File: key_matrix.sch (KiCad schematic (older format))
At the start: 168 parts

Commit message: Add LED controller + LEDS
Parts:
- added unit 2 of K_0_0
- added unit 2 of K_1_0
- added unit 2 of K_2_0
- added unit 2 of K_3_0
- added unit 2 of K_4_0
- added unit 2 of K_5_0
- added unit 2 of K_6_0
- added unit 2 of K_7_0
- added unit 2 of K_8_0
- added unit 2 of K_9_0
- added unit 2 of K_ALT1_0
- added unit 2 of K_ALT_0
- added unit 2 of K_A_0
- added unit 2 of K_BACKSPACE_0
- added unit 2 of K_BSLSH_0
- added unit 2 of K_B_0
- added unit 2 of K_CAPS_LOCK_0
- added unit 2 of K_COMMA_0
- added unit 2 of K_CTRL1_0
- added unit 2 of K_CTRL_0
- added unit 2 of K_C_0
- added unit 2 of K_DOT_0
- added unit 2 of K_DOWN_0
- added unit 2 of K_D_0
- added unit 2 of K_END_0
- added unit 2 of K_ENTER_0
- added unit 2 of K_EQUAL_0
- added unit 2 of K_ESC_0
- added unit 2 of K_E_0
- added unit 2 of K_F10_0
- added unit 2 of K_F11_0
- added unit 2 of K_F12_0
- added unit 2 of K_F1_0
- added unit 2 of K_F2_0
- added unit 2 of K_F3_0
- added unit 2 of K_F4_0
- added unit 2 of K_F5_0
- added unit 2 of K_F6_0
- added unit 2 of K_F7_0
- added unit 2 of K_F8_0
- added unit 2 of K_F9_0
- added unit 2 of K_FN_0
- added unit 2 of K_F_0
- added unit 2 of K_G_0
- added unit 2 of K_HOME_0
- added unit 2 of K_H_0
- added unit 2 of K_INSERT_0
- added unit 2 of K_I_0
- added unit 2 of K_J_0
- added unit 2 of K_K_0
- added unit 2 of K_LEFT_0
- added unit 2 of K_L_0
- added unit 2 of K_MINUS_0
- added unit 2 of K_M_0
- added unit 2 of K_NMLK_0
- added unit 2 of K_N_0
- added unit 2 of K_O_0
- added unit 2 of K_PAGE_DOWN_0
- added unit 2 of K_PAGE_UP_0
- added unit 2 of K_P_0
- added unit 2 of K_QUOTE_0
- added unit 2 of K_Q_0
- added unit 2 of K_RIGHT_0
- added unit 2 of K_R_0
- added unit 2 of K_SCRLK_0
- added unit 2 of K_SEMIC_0
- added unit 2 of K_SHIFT1_0
- added unit 2 of K_SHIFT_0
- added unit 2 of K_SLASH_0
- added unit 2 of K_SPC_0
- added unit 2 of K_S_0
- added unit 2 of K_TAB_0
- added unit 2 of K_T_0
- added unit 2 of K_UP_0
- added unit 2 of K_U_0
- added unit 2 of K_V_0
- added unit 2 of K_WIN_0
- added unit 2 of K_W_0
- added unit 2 of K_X_0
- added unit 2 of K_Y_0
- added unit 2 of K_Z_0
- added unit 2 of K_[_0
- added unit 2 of K_]_0
- added unit 2 of K_`_0
- K_0_0, K_1_0, K_2_0, K_3_0, K_4_0, K_5_0, K_6_0, K_7_0, K_8_0, K_9_0, K_ALT1_0, K_A_0, K_B_0, K_COMMA_0, K_CTRL1_0, K_C_0, K_DOT_0, K_DOWN_0, K_D_0, K_END_0, K_EQUAL_0, K_ESC_0, K_E_0, K_F10_0, K_F11_0, K_F12_0, K_F1_0, K_F2_0, K_F3_0, K_F4_0, K_F5_0, K_F6_0, K_F7_0, K_F8_0, K_F9_0, K_FN_0, K_F_0, K_G_0, K_HOME_0, K_H_0, K_INSERT_0, K_I_0, K_J_0, K_K_0, K_LEFT_0, K_L_0, K_MINUS_0, K_M_0, K_NMLK_0, K_N_0, K_O_0, K_PAGE_DOWN_0, K_PAGE_UP_0, K_P_0, K_QUOTE_0, K_Q_0, K_RIGHT_0, K_R_0, K_SCRLK_0, K_SEMIC_0, K_SLASH_0, K_S_0, K_T_0, K_UP_0, K_U_0, K_V_0, K_W_0, K_X_0, K_Y_0, K_Z_0, K_[_0, K_]_0, K_`_0: footprint MX_Alps_Hybrid:MX-1U-NoLED -> MX_Alps_Hybrid:MX-1U
- K_ALT_0, K_CTRL_0, K_WIN_0: footprint MX_Alps_Hybrid:MX-1.25U-NoLED -> MX_Alps_Hybrid:MX-1.25U
- K_BACKSPACE_0: footprint MX_Alps_Hybrid:MX-2U-NoLED -> MX_Alps_Hybrid:MX-2U
- K_BSLSH_0, K_TAB_0: footprint MX_Alps_Hybrid:MX-1.5U-NoLED -> MX_Alps_Hybrid:MX-1.5U
- K_CAPS_LOCK_0, K_SHIFT1_0: footprint MX_Alps_Hybrid:MX-1.75U-NoLED -> MX_Alps_Hybrid:MX-1.75U
- K_ENTER_0, K_SHIFT_0: footprint MX_Alps_Hybrid:MX-2.25U-NoLED -> MX_Alps_Hybrid:MX-2.25U
- K_SPC_0: footprint MX_Alps_Hybrid:MX-6.25U-NoLED -> MX_Alps_Hybrid:MX-6.25U
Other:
- note added: "White LEDs, approx 3.3V Vf"

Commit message: Wire LEDs into controller
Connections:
- net LED_CB2: now reaches K_L_0.3 (A)
- net LED_CB2: now also K_0_0.4 (K), K_8_0.4 (K), K_9_0.4 (K), K_BACKSPACE_0.4 (K), K_DOT_0.3 (A), K_EQUAL_0.4 (K), K_F8_0.3 (A), K_HOME_0.4 (K), K_MINUS_0.4 (K), K_O_0.3 (A), K_RIGHT_0.3 (A)
- net LED_CB4: now reaches K_L_0.4 (K)
- net LED_CB4: now also K_0_0.3 (A), K_ENTER_0.4 (K), K_F10_0.3 (A), K_K_0.4 (K), K_PAGE_DOWN_0.4 (K), K_P_0.3 (A), K_QUOTE_0.4 (K), K_SEMIC_0.4 (K), K_SHIFT1_0.3 (A)
- net LED_CA9: now reaches K_M_0.3 (A)
- net LED_CA9: now also K_7_0.3 (A), K_F7_0.3 (A), K_J_0.3 (A), K_LEFT_0.3 (A), K_U_0.3 (A)
- net LED_CA5: now reaches K_M_0.4 (K)
- net LED_CA5: now also K_3_0.3 (A), K_ALT1_0.3 (A), K_B_0.4 (K), K_C_0.4 (K), K_D_0.3 (A), K_E_0.3 (A), K_F3_0.3 (A), K_N_0.4 (K), K_SHIFT_0.4 (K), K_V_0.4 (K), K_X_0.4 (K), K_Z_0.4 (K)
- net LED_CB3: now reaches K_O_0.4 (K)
- net LED_CB3: now also K_9_0.3 (A), K_BSLSH_0.4 (K), K_F9_0.3 (A), K_I_0.4 (K), K_PAGE_UP_0.4 (K), K_P_0.4 (K), K_SEMIC_0.3 (A), K_SLASH_0.3 (A), K_[_0.4 (K), K_]_0.4 (K)
- net LED_CB1: now reaches K_COMMA_0.3 (A)
- net LED_CB1: now also K_8_0.3 (A), K_DOWN_0.3 (A), K_F10_0.4 (K), K_F11_0.4 (K), K_F12_0.4 (K), K_F8_0.4 (K), K_F9_0.4 (K), K_INSERT_0.4 (K), K_I_0.3 (A), K_K_0.3 (A), K_NMLK_0.4 (K), K_SCRLK_0.4 (K)
- net LED_CB5: now reaches K_COMMA_0.4 (K)
- net LED_CB5: now also K_DOT_0.4 (K), K_END_0.4 (K), K_F11_0.3 (A), K_MINUS_0.3 (A), K_QUOTE_0.3 (A), K_SHIFT1_0.4 (K), K_SLASH_0.4 (K), K_UP_0.4 (K), K_[_0.3 (A)
- net LED_CA8: now reaches K_N_0.3 (A)
- net LED_CA8: now also K_6_0.3 (A), K_CTRL1_0.3 (A), K_F6_0.3 (A), K_H_0.3 (A), K_Y_0.3 (A)
- net LED_CA2: now reaches K_Z_0.3 (A)
- net LED_CA2: now also K_1_0.4 (K), K_2_0.4 (K), K_3_0.4 (K), K_4_0.4 (K), K_5_0.4 (K), K_6_0.4 (K), K_7_0.4 (K), K_A_0.3 (A), K_ESC_0.3 (A), K_Q_0.3 (A), K_WIN_0.3 (A), K_`_0.4 (K)
- net LED_CA3: now reaches K_F1_0.3 (A)
- net LED_CA3: now also K_1_0.3 (A), K_ALT_0.3 (A), K_E_0.4 (K), K_Q_0.4 (K), K_R_0.4 (K), K_S_0.3 (A), K_TAB_0.4 (K), K_T_0.4 (K), K_U_0.4 (K), K_W_0.4 (K), K_X_0.3 (A), K_Y_0.4 (K)
- net LED_CA1: now reaches K_F1_0.4 (K)
- net LED_CA1: now also K_CAPS_LOCK_0.3 (A), K_CTRL_0.3 (A), K_ESC_0.4 (K), K_F2_0.4 (K), K_F3_0.4 (K), K_F4_0.4 (K), K_F5_0.4 (K), K_F6_0.4 (K), K_F7_0.4 (K), K_SHIFT_0.3 (A), K_TAB_0.3 (A), K_`_0.3 (A)
- net LED_CA7: now reaches K_B_0.3 (A)
- net LED_CA7: now also K_5_0.3 (A), K_F5_0.3 (A), K_FN_0.3 (A), K_G_0.3 (A), K_T_0.3 (A)
- net LED_CA6: now reaches K_V_0.3 (A)
- net LED_CA6: now also K_4_0.3 (A), K_ALT1_0.4 (K), K_ALT_0.4 (K), K_CTRL1_0.4 (K), K_CTRL_0.4 (K), K_F4_0.3 (A), K_FN_0.4 (K), K_F_0.3 (A), K_LEFT_0.4 (K), K_R_0.3 (A), K_SPC_0.4 (K), K_WIN_0.4 (K)
- net LED_CA4: now reaches K_C_0.3 (A)
- net LED_CA4: now also K_2_0.3 (A), K_A_0.4 (K), K_CAPS_LOCK_0.4 (K), K_D_0.4 (K), K_F2_0.3 (A), K_F_0.4 (K), K_G_0.4 (K), K_H_0.4 (K), K_J_0.4 (K), K_SPC_0.3 (A), K_S_0.4 (K), K_W_0.3 (A)
- net LED_CB6: now reaches K_UP_0.3 (A)
- net LED_CB6: now also K_DOWN_0.4 (K), K_ENTER_0.3 (A), K_EQUAL_0.3 (A), K_F12_0.3 (A), K_RIGHT_0.4 (K), K_]_0.3 (A)
- net LED_CB7: now reaches K_END_0.3 (A)
- net LED_CB7: now also K_BACKSPACE_0.3 (A), K_BSLSH_0.3 (A), K_PAGE_DOWN_0.3 (A), K_SCRLK_0.3 (A)
- net LED_CB8: now reaches K_PAGE_UP_0.3 (A)
- net LED_CB8: now also K_HOME_0.3 (A), K_NMLK_0.3 (A)
- net LED_CB9: now reaches K_INSERT_0.3 (A)

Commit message: Ripup all traces, rewire schematic matrix to better fit pcb layout
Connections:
- net LED_CA2: no longer K_A_0.3 (A), K_Q_0.3 (A), K_Z_0.3 (A)
- net LED_CA3: now also K_A_0.3 (A), K_Z_0.3 (A); no longer K_S_0.3 (A), K_U_0.4 (K), K_X_0.3 (A)
- net LED_CA4: now also K_Q_0.3 (A), K_X_0.3 (A); no longer K_C_0.3 (A), K_J_0.4 (K), K_SPC_0.3 (A), K_W_0.3 (A)
- net LED_CA5: now also K_S_0.3 (A), K_W_0.3 (A); no longer K_ALT1_0.3 (A), K_D_0.3 (A), K_E_0.3 (A), K_M_0.4 (K)
- net LED_CA6: now also K_C_0.3 (A), K_D_0.3 (A), K_E_0.3 (A); no longer K_ALT1_0.4 (K), K_CTRL1_0.4 (K), K_FN_0.4 (K), K_F_0.3 (A), K_LEFT_0.4 (K), K_R_0.3 (A), K_V_0.3 (A)
- net LED_CA7: now also K_F_0.3 (A), K_R_0.3 (A), K_V_0.3 (A); no longer K_B_0.3 (A), K_FN_0.3 (A), K_G_0.3 (A), K_T_0.3 (A)
- net LED_CA8: now also K_B_0.3 (A), K_G_0.3 (A), K_SPC_0.3 (A), K_T_0.3 (A); no longer K_CTRL1_0.3 (A), K_H_0.3 (A), K_N_0.3 (A), K_Y_0.3 (A)
- net LED_CA9: now also K_H_0.3 (A), K_N_0.3 (A), K_Y_0.3 (A); no longer K_J_0.3 (A), K_LEFT_0.3 (A), K_M_0.3 (A), K_U_0.3 (A)
- net LED_CB1: now also K_J_0.3 (A), K_M_0.3 (A), K_U_0.3 (A); no longer K_COMMA_0.3 (A), K_DOWN_0.3 (A), K_I_0.3 (A), K_K_0.3 (A)
- net LED_CB2: now also K_COMMA_0.3 (A), K_I_0.3 (A), K_K_0.3 (A); no longer K_DOT_0.3 (A), K_L_0.3 (A), K_O_0.3 (A), K_RIGHT_0.3 (A)
- net LED_CB3: now also K_ALT1_0.3 (A), K_DOT_0.3 (A), K_L_0.3 (A), K_U_0.4 (K); no longer K_SEMIC_0.3 (A), K_SLASH_0.3 (A)
- net LED_CB4: now also K_FN_0.3 (A), K_J_0.4 (K), K_O_0.3 (A), K_SLASH_0.3 (A); no longer K_P_0.3 (A), K_SHIFT1_0.3 (A)
- net LED_CB5: now also K_CTRL1_0.3 (A), K_M_0.4 (K), K_P_0.3 (A), K_SEMIC_0.3 (A); no longer K_QUOTE_0.3 (A), K_[_0.3 (A)
- net LED_CB6: now also K_ALT1_0.4 (K), K_CTRL1_0.4 (K), K_FN_0.4 (K), K_LEFT_0.4 (K), K_QUOTE_0.3 (A), K_[_0.3 (A); no longer K_ENTER_0.3 (A), K_UP_0.3 (A), K_]_0.3 (A)
- net LED_CB7: now also K_LEFT_0.3 (A), K_SHIFT1_0.3 (A), K_]_0.3 (A); no longer K_BACKSPACE_0.3 (A), K_BSLSH_0.3 (A), K_END_0.3 (A), K_PAGE_DOWN_0.3 (A)
- net LED_CB8: now also K_BACKSPACE_0.3 (A), K_BSLSH_0.3 (A), K_DOWN_0.3 (A), K_ENTER_0.3 (A), K_UP_0.3 (A); no longer K_HOME_0.3 (A), K_PAGE_UP_0.3 (A)
- net LED_CB9: now also K_END_0.3 (A), K_HOME_0.3 (A), K_PAGE_DOWN_0.3 (A), K_PAGE_UP_0.3 (A), K_RIGHT_0.3 (A)
- net col1: no longer K_A_0.1, K_Q_0.1, K_Z_0.1
- net col10: now also K_ALT1_0.1, K_DOT_0.1, K_L_0.1, K_O_0.1; no longer K_P_0.1, K_SEMIC_0.1, K_SLASH_0.1
- net col11: now also K_FN_0.1, K_P_0.1, K_SEMIC_0.1, K_SLASH_0.1; no longer K_QUOTE_0.1, K_SHIFT1_0.1, K_[_0.1
- net col12: now also K_CTRL1_0.1, K_QUOTE_0.1, K_[_0.1; no longer K_ENTER_0.1, K_UP_0.1, K_]_0.1
- net col13: now also K_LEFT_0.1, K_SHIFT1_0.1, K_]_0.1; no longer K_BACKSPACE_0.1, K_BSLSH_0.1, K_END_0.1, K_PAGE_DOWN_0.1
- net col14: now also K_BACKSPACE_0.1, K_BSLSH_0.1, K_DOWN_0.1, K_ENTER_0.1, K_UP_0.1; no longer K_HOME_0.1, K_PAGE_UP_0.1
- net col15: now also K_END_0.1, K_HOME_0.1, K_PAGE_DOWN_0.1, K_PAGE_UP_0.1, K_RIGHT_0.1
- net col2: now also K_A_0.1, K_Q_0.1, K_Z_0.1; no longer K_S_0.1, K_W_0.1, K_X_0.1
- net col3: now also K_S_0.1, K_W_0.1, K_X_0.1; no longer K_C_0.1, K_D_0.1, K_E_0.1, K_SPC_0.1
- net col4: now also K_C_0.1, K_D_0.1, K_E_0.1; no longer K_ALT1_0.1, K_F_0.1, K_R_0.1, K_V_0.1
- net col5: now also K_F_0.1, K_R_0.1, K_V_0.1; no longer K_B_0.1, K_FN_0.1, K_G_0.1, K_T_0.1
- net col6: now also K_B_0.1, K_G_0.1, K_SPC_0.1, K_T_0.1; no longer K_CTRL1_0.1, K_H_0.1, K_N_0.1, K_Y_0.1
- net col7: now also K_H_0.1, K_N_0.1, K_Y_0.1; no longer K_J_0.1, K_LEFT_0.1, K_M_0.1, K_U_0.1
- net col8: now also K_J_0.1, K_M_0.1, K_U_0.1; no longer K_COMMA_0.1, K_DOWN_0.1, K_I_0.1, K_K_0.1
- net col9: now also K_COMMA_0.1, K_I_0.1, K_K_0.1; no longer K_DOT_0.1, K_L_0.1, K_O_0.1, K_RIGHT_0.1
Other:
- moved on the sheet: D_ALT1_0, D_A_0, D_BACKSPACE_0, D_BSLSH_0, D_B_0, D_COMMA_0, D_CTRL1_0, D_C_0, D_DOT_0, D_DOWN_0, D_D_0, D_END_0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

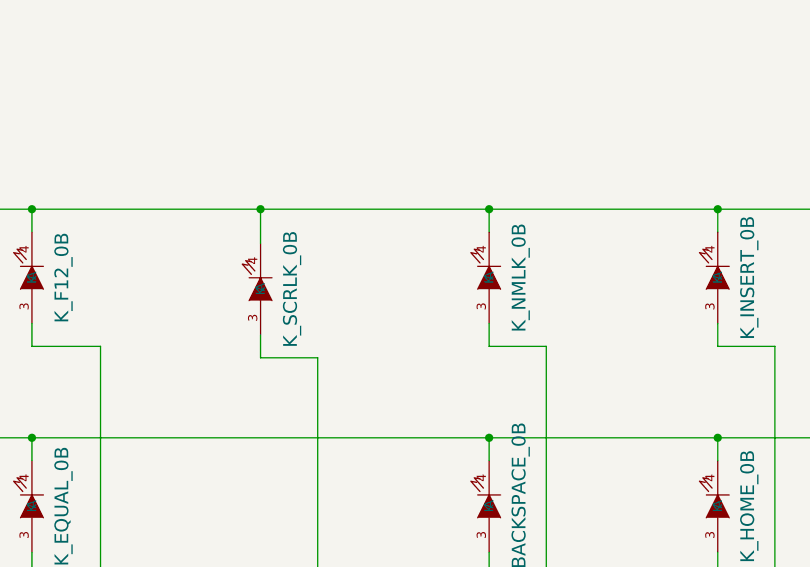
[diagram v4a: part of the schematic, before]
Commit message: Rewire as 4 layer board
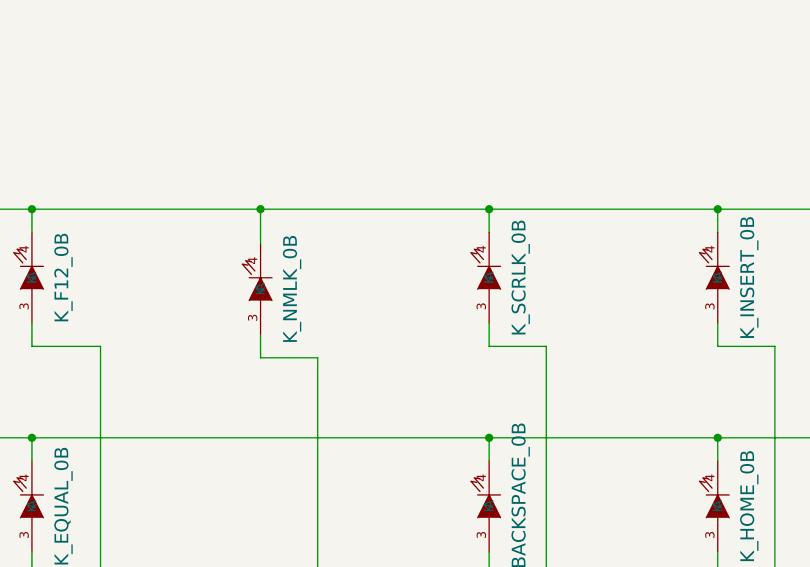
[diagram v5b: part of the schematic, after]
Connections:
- net LED_CB7: now also K_NMLK_0.3 (A); no longer K_SCRLK_0.3 (A)
- net LED_CB8: now also K_SCRLK_0.3 (A); no longer K_NMLK_0.3 (A)
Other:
- moved on the sheet: K_NMLK_0B, K_SCRLK_0B
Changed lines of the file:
@@
 L keyboard_parts:KEYSW K_SCRLK_0
 U 2 1 5E754C95
+P 16000 9250
+F 0 "K_SCRLK_0" H 16000 9381 60  0000 C CNN
+F 1 "KEYSW" H 16000 9100 60  0001 C CNN
+F 2 "MX_Alps_Hybrid:MX-1U" H 16000 9250 60  0001 C CNN
+F 3 "" H 16000 9250 60  0000 C CNN
+	2    16000 9250
+	0    1    1    0
+$EndComp
+$Comp
+L keyboard_parts:KEYSW K_NMLK_0
+U 2 1 5E754C97
 P 15000 9300
-F 0 "K_SCRLK_0" H 15000 9431 60  0000 C CNN
+F 0 "K_NMLK_0" H 15000 9431 60  0000 C CNN
 F 1 "KEYSW" H 15000 9150 60  0001 C CNN
 F 2 "MX_Alps_Hybrid:MX-1U" H 15000 9300 60  0001 C CNN
@@
 	0    1    1    0
 $EndComp
-$Comp
-L keyboard_parts:KEYSW K_NMLK_0
-U 2 1 5E754C97
-P 16000 9250
-F 0 "K_NMLK_0" H 16000 9381 60  0000 C CNN
-F 1 "KEYSW" H 16000 9100 60  0001 C CNN
-F 2 "MX_Alps_Hybrid:MX-1U" H 16000 9250 60  0001 C CNN
-F 3 "" H 16000 9250 60  0000 C CNN
-	2    16000 9250
-	0    1    1    0
-$EndComp

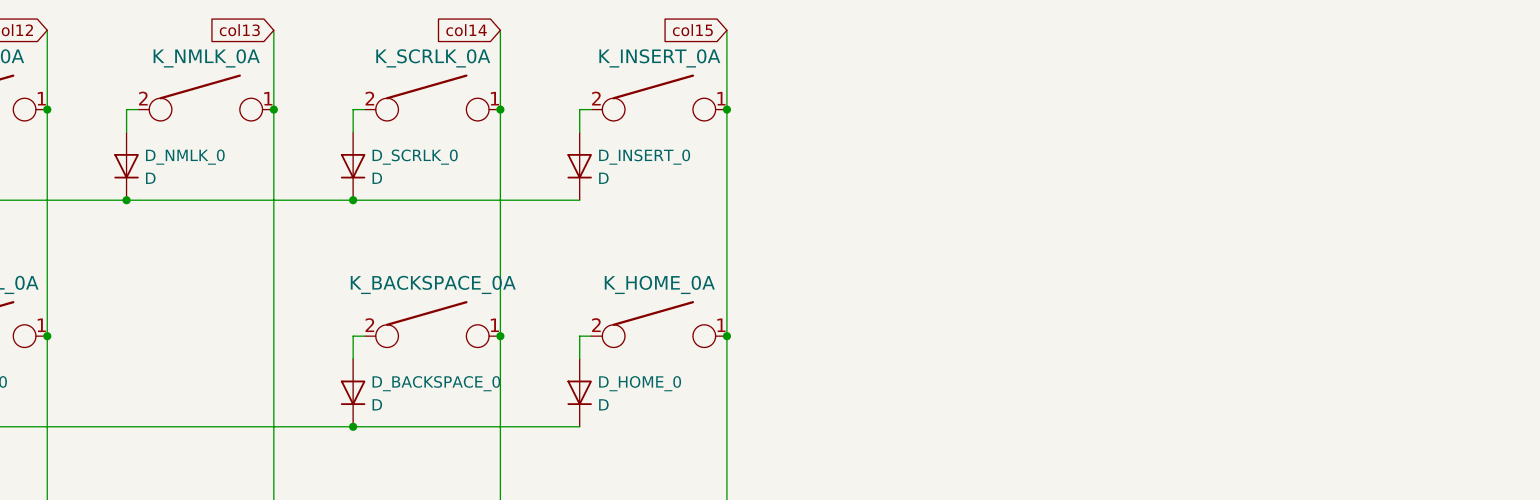
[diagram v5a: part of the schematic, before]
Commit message: Add display and encoder
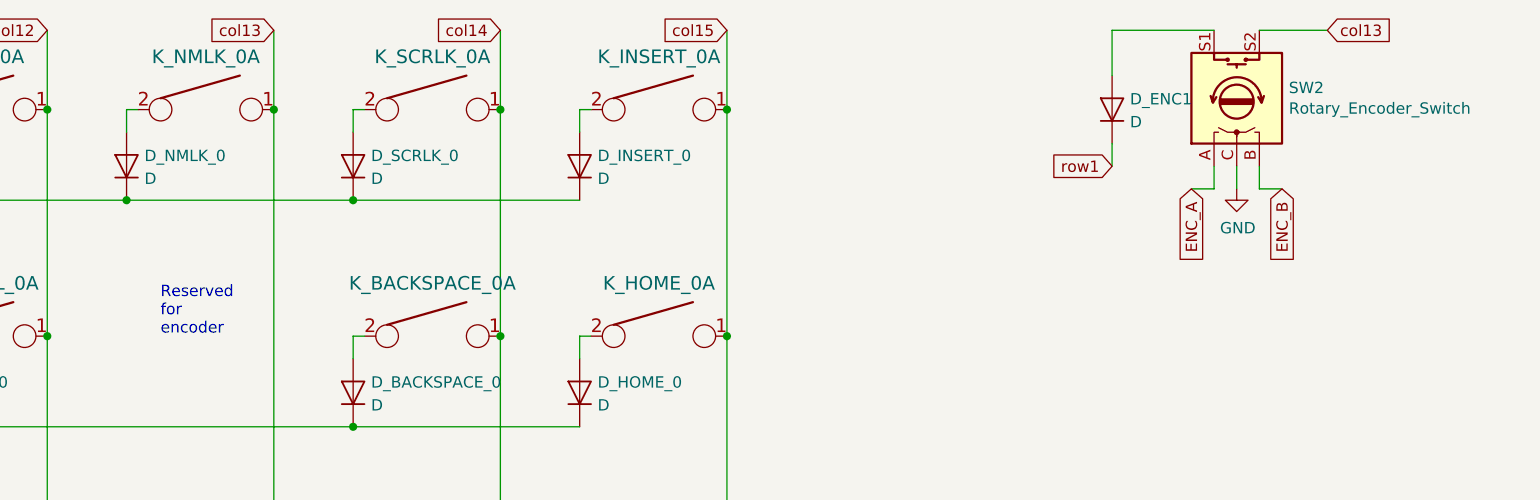
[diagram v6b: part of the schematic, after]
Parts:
- added D_ENC1: D, keyboard_parts:D_SOD123_axial, symbol Device:D
- added SW2: Rotary_Encoder_Switch, bluebird:482016514001, symbol Device:Rotary_Encoder_Switch
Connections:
- net col13: now also SW2.S2
- net row1: now also D_ENC1.1 (K)
- new net: D_ENC1.2 (A), SW2.S1
- new net ENC_A: SW2.A
- new net ENC_B: SW2.B
- new net GND: SW2.C
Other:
- note added: "Reserved \nfor\nencoder"
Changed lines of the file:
@@
 	11250 14550 11250 13550
 Connection ~ 11250 13550
+$Comp
+L Device:Rotary_Encoder_Switch SW2
+U 1 1 5E85CF73
+P 19550 1950
+F 0 "SW2" V 19596 1720 50  0000 R CNN
+F 1 "Rotary_Encoder_Switch" V 19505 1720 50  0000 R CNN
+F 2 "bluebird:482016514001" H 19400 2110 50  0001 C CNN
+F 3 "~" H 19550 2210 50  0001 C CNN
+	1    19550 1950
+	0    -1   -1   0
+$EndComp
+Text GLabel 19350 2350 3    50   Input ~ 0
+ENC_A
+Text GLabel 19750 2350 3    50   Input ~ 0
+ENC_B
+Wire Wire Line
+	19450 2250 19450 2350
+Wire Wire Line
+	19450 2350 19350 2350
+Wire Wire Line
+	19650 2250 19650 2350
+Wire Wire Line
+	19650 2350 19750 2350
+$Comp
+L power:GND #PWR0111
+U 1 1 5EB6B512
+P 19550 2350
+F 0 "#PWR0111" H 19550 2100 50  0001 C CNN
+F 1 "GND" H 19555 2177 50  0000 C CNN
+F 2 "" H 19550 2350 50  0001 C CNN
+F 3 "" H 19550 2350 50  0001 C CNN
+	1    19550 2350
+	1    0    0    -1
+$EndComp
+Wire Wire Line
+	19550 2250 19550 2350
+Text GLabel 19950 1650 2    50   Input ~ 0
+col13
+$Comp
+L Device:D D_ENC1
+U 1 1 5EC0A494
+P 19000 2000
+F 0 "D_ENC1" V 19046 1921 50  0000 R CNN
+F 1 "D" V 18945 1921 50  0000 R CNN
+F 2 "keyboard_parts:D_SOD123_axial" H 19000 2000 50  0001 C CNN
+F 3 "~" H 19000 2000 50  0001 C CNN
+	1    19000 2000
+	0    -1   -1   0
+$EndComp
+Wire Wire Line
+	19450 1650 19000 1650
+Wire Wire Line
+	19000 1650 19000 1850
+Wire Wire Line
+	19650 1650 19950 1650
+Text GLabel 19000 2250 0    50   Input ~ 0
+row1
+Wire Wire Line
+	19000 2150 19000 2250
+Text Notes 14800 3000 0    50   ~ 0
+Reserved \nfor\nencoder
 $EndSCHEMATC

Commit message: Rewire as 2 layer numpad
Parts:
- removed D_0_0, D_1_0, D_2_0, D_3_0, D_4_0, D_6_0, D_7_0, D_8_0, D_9_0, D_ALT1_0, D_ALT_0, D_A_0, D_BACKSPACE_0, D_BSLSH_0, D_B_0, D_CAPS_LOCK_0, D_COMMA_0, D_CTRL1_0, D_CTRL_0, D_C_0, D_DOT_0, D_D_0, D_ENC1, D_EQUAL_0, D_ESC_0, D_E_0, D_F10_0, D_F11_0, D_F12_0, D_F1_0, D_F2_0, D_F3_0, D_F4_0, D_F5_0, D_F6_0, D_F7_0, D_F8_0, D_F9_0, D_FN_0, D_F_0, D_G_0, D_H_0, D_INSERT_0, D_I_0, D_J_0, D_K_0, D_L_0, D_M_0, D_NMLK_0, D_N_0, D_O_0, D_PAGE_DOWN_0, D_PAGE_UP_0, D_P_0, D_QUOTE_0, D_Q_0, D_R_0, D_SCRLK_0, D_SEMIC_0, D_SHIFT1_0, D_SHIFT_0, D_SPC_0, D_S_0, D_TAB_0, D_T_0, D_U_0, D_V_0, D_WIN_0, D_W_0, D_X_0, D_Y_0, D_Z_0, D_[_0, D_]_0, D_`_0: D, keyboard_parts:D_SOD123_axial, symbol Device:D
- removed K_0_0, K_1_0, K_2_0, K_3_0, K_4_0, K_6_0, K_7_0, K_8_0, K_9_0, K_ALT1_0, K_A_0, K_B_0, K_COMMA_0, K_CTRL1_0, K_C_0, K_DOT_0, K_D_0, K_EQUAL_0, K_ESC_0, K_E_0, K_F10_0, K_F11_0, K_F12_0, K_F1_0, K_F2_0, K_F3_0, K_F4_0, K_F5_0, K_F6_0, K_F7_0, K_F8_0, K_F9_0, K_FN_0, K_F_0, K_G_0, K_H_0, K_INSERT_0, K_I_0, K_J_0, K_K_0, K_M_0, K_NMLK_0, K_N_0, K_O_0, K_PAGE_DOWN_0, K_PAGE_UP_0, K_P_0, K_QUOTE_0, K_Q_0, K_R_0, K_SCRLK_0, K_SEMIC_0, K_S_0, K_T_0, K_U_0, K_V_0, K_W_0, K_X_0, K_Y_0, K_Z_0, K_[_0, K_]_0, K_`_0: KEYSW, MX_Alps_Hybrid:MX-1U, symbol keyboard_parts:KEYSW
- removed K_ALT_0, K_CTRL_0, K_WIN_0: KEYSW, MX_Alps_Hybrid:MX-1.25U, symbol keyboard_parts:KEYSW
- removed K_BACKSPACE_0: KEYSW, MX_Alps_Hybrid:MX-2U, symbol keyboard_parts:KEYSW
- removed K_BSLSH_0, K_TAB_0: KEYSW, MX_Alps_Hybrid:MX-1.5U, symbol keyboard_parts:KEYSW
- removed K_CAPS_LOCK_0, K_SHIFT1_0: KEYSW, MX_Alps_Hybrid:MX-1.75U, symbol keyboard_parts:KEYSW
- removed unit 2 of K_LEFT_0
- removed unit 1 of K_L_0
- removed K_SHIFT_0: KEYSW, MX_Alps_Hybrid:MX-2.25U, symbol keyboard_parts:KEYSW
- removed K_SPC_0: KEYSW, MX_Alps_Hybrid:MX-6.25U, symbol keyboard_parts:KEYSW
- removed SW2: Rotary_Encoder_Switch, bluebird:482016514001, symbol Device:Rotary_Encoder_Switch
- added D_*_0, D_+_0, D_DEL_0, D_INS_0, D_NUM_LOCK_0, D_PGDN_0, D_PGUP_0: D, keyboard_parts:D_SOD123_axial, symbol Device:D
- added K_*_0, K_DEL_0, K_NUM_LOCK_0, K_PGDN_0, K_PGUP_0: KEYSW, MX_Alps_Hybrid:MX-1U, symbol keyboard_parts:KEYSW
- added K_+_0, K_INS_0: KEYSW, MX_Alps_Hybrid:MX-2U, symbol keyboard_parts:KEYSW
- K_ENTER_0: footprint MX_Alps_Hybrid:MX-2.25U -> MX_Alps_Hybrid:MX-2U
- renumbered K_L_0 to K_LEFT_0
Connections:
- net LED_CA7 is gone; now on net LED_CA2: K_5_0.3 (A)
- net LED_CB3 is gone; now on net LED_CA1: K_LEFT_0.3 (A)
- net col13 is gone; now on net col0: K_LEFT_0.1
- net col5 is gone; now on net col1: K_5_0.1
- net LED_CA1: now also K_END_0.3 (A), K_HOME_0.3 (A), K_MINUS_0.4 (K), K_SLASH_0.4 (K), K_*_0.4 (K), K_INS_0.3 (A), K_NUM_LOCK_0.4 (K)
- net LED_CA2: now also K_DOWN_0.3 (A), K_HOME_0.4 (K), K_UP_0.4 (K), K_NUM_LOCK_0.3 (A), K_PGUP_0.4 (K); no longer K_5_0.4 (K)
- net LED_CA3: now also K_5_0.4 (K), K_LEFT_0.4 (K), K_RIGHT_0.4 (K), K_SLASH_0.3 (A), K_UP_0.3 (A), K_+_0.4 (K), K_DEL_0.3 (A), K_PGDN_0.3 (A)
- net LED_CA4: now also K_DOWN_0.4 (K), K_END_0.4 (K), K_ENTER_0.3 (A), K_RIGHT_0.3 (A), K_*_0.3 (A), K_PGDN_0.4 (K), K_PGUP_0.3 (A)
- net LED_CA5: now also K_ENTER_0.4 (K), K_MINUS_0.3 (A), K_+_0.3 (A), K_DEL_0.4 (K), K_INS_0.4 (K)
- net col0: now also K_END_0.1, K_HOME_0.1, K_INS_0.1, K_NUM_LOCK_0.1
- net col1: now also K_DOWN_0.1, K_SLASH_0.1, K_UP_0.1
- net col2: now also K_RIGHT_0.1, K_*_0.1, K_DEL_0.1, K_PGDN_0.1, K_PGUP_0.1
- net col3: now also K_ENTER_0.1, K_MINUS_0.1, K_+_0.1
- net row0: now also D_MINUS_0.1 (K), D_SLASH_0.1 (K), D_*_0.1 (K), D_NUM_LOCK_0.1 (K)
- net row1: now also D_UP_0.1 (K), D_+_0.1 (K), D_PGUP_0.1 (K); no longer D_5_0.1 (K), D_MINUS_0.1 (K)
- net row2: now also D_5_0.1 (K), D_LEFT_0.1 (K), D_RIGHT_0.1 (K)
- net row3: now also D_DOWN_0.1 (K), D_END_0.1 (K), D_PGDN_0.1 (K)
- net row4: now also D_DEL_0.1 (K), D_INS_0.1 (K); no longer D_END_0.1 (K), D_SLASH_0.1 (K), D_UP_0.1 (K)
- removed net LED_CB2: K_HOME_0.4 (K), K_MINUS_0.4 (K)
- removed net LED_CB4: K_ENTER_0.4 (K), K_LEFT_0.4 (K), K_SLASH_0.3 (A)
- removed net LED_CB5: K_END_0.4 (K), K_MINUS_0.3 (A), K_SLASH_0.4 (K), K_UP_0.4 (K)
- removed net LED_CB6: K_DOWN_0.4 (K), K_RIGHT_0.4 (K)
- removed net LED_CB8: K_DOWN_0.3 (A), K_ENTER_0.3 (A), K_UP_0.3 (A)
- removed net LED_CB9: K_END_0.3 (A), K_HOME_0.3 (A), K_RIGHT_0.3 (A)
- removed net col11: K_MINUS_0.1, K_SLASH_0.1
- removed net col14: K_DOWN_0.1, K_ENTER_0.1, K_UP_0.1
- removed net col15: K_END_0.1, K_HOME_0.1, K_RIGHT_0.1
- removed net row5: D_DOWN_0.1 (K), D_LEFT_0.1 (K), D_RIGHT_0.1 (K)
- new net: D_PGDN_0.2 (A), K_PGDN_0.2
- new net: D_NUM_LOCK_0.2 (A), K_NUM_LOCK_0.2
- new net: D_DEL_0.2 (A), K_DEL_0.2
- new net: D_INS_0.2 (A), K_INS_0.2
- new net: D_+_0.2 (A), K_+_0.2
- new net: D_PGUP_0.2 (A), K_PGUP_0.2
- new net: D_*_0.2 (A), K_*_0.2
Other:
- note removed: "Reserved \nfor\nencoder"
- note removed: "White LEDs, approx 3.3V Vf"
- moved on the sheet: K_LEFT_0B
